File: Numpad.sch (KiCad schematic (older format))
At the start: 51 parts, among them J1 USB_B_Mini, SW0 0, SW1 1, SW2 2, SW3 3, SW4 4, SW5 5, SW6 6, SW7 7, SW8 8, SW9 9, U1 ATmega32U4-AU, Y1 16MHz

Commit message: plate files added, moved around some more components
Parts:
- C6: value 0.1uF -> 1uF
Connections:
- net Col1: now also U1.29 (PB5); no longer U1.18 (PD0)
- net Col2: now also U1.28 (PB4); no longer U1.19 (PD1)
- net Col3: now also U1.26 (PD6); no longer U1.20 (PD2)
- net Col4: now also U1.25 (PD4); no longer U1.21 (PD3)
- net Row1: now also U1.41 (PF0); no longer U1.8 (PB0)
- net Row2: now also U1.40 (PF1); no longer U1.9 (PB1)
- net Row3: now also U1.39 (PF4); no longer U1.10 (PB2)
- net Row4: now also U1.38 (PF5); no longer U1.11 (PB3)
- net Row5: now also U1.37 (PF6); no longer U1.28 (PB4)
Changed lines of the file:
@@
 	0    -1   -1   0
-$EndComp
-$Comp
-L Device:C_Small C5
-U 1 1 5D759123
-P 3600 1300
-F 0 "C5" V 3829 1300 50  0000 C CNN
-F 1 "10uF" V 3738 1300 50  0000 C CNN
-F 2 "Capacitor_SMD:C_0805_2012Metric_Pad1.15x1.40mm_HandSolder" H 3600 1300 50  0001 C CNN
-F 3 "~" H 3600 1300 50  0001 C CNN
-	1    3600 1300
-	-1   0    0    1
-$EndComp
-$Comp
-L Device:C_Small C6
-U 1 1 5D759CD2
-P 3950 1300
-F 0 "C6" V 4179 1300 50  0000 C CNN
-F 1 "0.1uF" V 4088 1300 50  0000 C CNN
-F 2 "Capacitor_SMD:C_0805_2012Metric_Pad1.15x1.40mm_HandSolder" H 3950 1300 50  0001 C CNN
-F 3 "~" H 3950 1300 50  0001 C CNN
-	1    3950 1300
-	-1   0    0    1
-$EndComp
-$Comp
-L Device:C_Small C8
-U 1 1 5D75B0ED
-P 4650 1300
-F 0 "C8" V 4879 1300 50  0000 C CNN
-F 1 "01.uF" V 4788 1300 50  0000 C CNN
-F 2 "Capacitor_SMD:C_0805_2012Metric_Pad1.15x1.40mm_HandSolder" H 4650 1300 50  0001 C CNN
-F 3 "~" H 4650 1300 50  0001 C CNN
-	1    4650 1300
-	-1   0    0    1
 $EndComp
 Wire Wire Line
@@
 	4650 1600 4300 1600
 Connection ~ 4300 1600
-$Comp
-L Device:C_Small C7
-U 1 1 5D75A7CA
-P 4300 1300
-F 0 "C7" V 4529 1300 50  0000 C CNN
-F 1 "0.1uF" V 4438 1300 50  0000 C CNN
-F 2 "Capacitor_SMD:C_0805_2012Metric_Pad1.15x1.40mm_HandSolder" H 4300 1300 50  0001 C CNN
-F 3 "~" H 4300 1300 50  0001 C CNN
-	1    4300 1300
-	-1   0    0    1
-$EndComp
 $Comp
 L Device:R_Small R1
@@
 Wire Wire Line
 	2600 6900 2600 6800
-Text GLabel 1300 5300 1    50   Output ~ 0
+Text GLabel 3700 5300 1    50   Output ~ 0
 Row1
-Text GLabel 1400 5300 1    50   Output ~ 0
+Text GLabel 3800 5300 1    50   Output ~ 0
 Row2
-Text GLabel 1500 5300 1    50   Output ~ 0
+Text GLabel 3900 5300 1    50   Output ~ 0
 Row3
-Text GLabel 1600 5300 1    50   Output ~ 0
+Text GLabel 4000 5300 1    50   Output ~ 0
 Row4
+Text GLabel 4100 5300 1    50   Output ~ 0
+Row5
+Text GLabel 1800 5300 1    50   Output ~ 0
+Col1
 Text GLabel 1700 5300 1    50   Output ~ 0
-Row5
-Text GLabel 2500 5300 1    50   Output ~ 0
-Col1
-Text GLabel 2600 5300 1    50   Output ~ 0
 Col2
-Text GLabel 2700 5300 1    50   Output ~ 0
+Text GLabel 3100 5300 1    50   Output ~ 0
 Col3
-Text GLabel 2800 5300 1    50   Output ~ 0
+Text GLabel 2900 5300 1    50   Output ~ 0
 Col4
 Text GLabel 2300 6500 3    50   Input ~ 0
@@
 Wire Wire Line
 	2850 2700 2850 2550
+$Comp
+L Device:C_Small C8
+U 1 1 5D75B0ED
+P 4650 1300
+F 0 "C8" V 4879 1300 50  0000 C CNN
+F 1 "01.uF" V 4788 1300 50  0000 C CNN
+F 2 "Capacitor_SMD:C_0805_2012Metric_Pad1.15x1.40mm_HandSolder" H 4650 1300 50  0001 C CNN
+F 3 "~" H 4650 1300 50  0001 C CNN
+	1    4650 1300
+	-1   0    0    1
+$EndComp
+$Comp
+L Device:C_Small C7
+U 1 1 5D75A7CA
+P 4300 1300
+F 0 "C7" V 4529 1300 50  0000 C CNN
+F 1 "0.1uF" V 4438 1300 50  0000 C CNN
+F 2 "Capacitor_SMD:C_0805_2012Metric_Pad1.15x1.40mm_HandSolder" H 4300 1300 50  0001 C CNN
+F 3 "~" H 4300 1300 50  0001 C CNN
+	1    4300 1300
+	-1   0    0    1
+$EndComp
+$Comp
+L Device:C_Small C6
+U 1 1 5D759CD2
+P 3950 1300
+F 0 "C6" V 4179 1300 50  0000 C CNN
+F 1 "1uF" V 4088 1300 50  0000 C CNN
+F 2 "Capacitor_SMD:C_0805_2012Metric_Pad1.15x1.40mm_HandSolder" H 3950 1300 50  0001 C CNN
+F 3 "~" H 3950 1300 50  0001 C CNN
+	1    3950 1300
+	-1   0    0    1
+$EndComp
+$Comp
+L Device:C_Small C5
+U 1 1 5D759123
+P 3600 1300
+F 0 "C5" V 3829 1300 50  0000 C CNN
+F 1 "10uF" V 3738 1300 50  0000 C CNN
+F 2 "Capacitor_SMD:C_0805_2012Metric_Pad1.15x1.40mm_HandSolder" H 3600 1300 50  0001 C CNN
+F 3 "~" H 3600 1300 50  0001 C CNN
+	1    3600 1300
+	-1   0    0    1
+$EndComp
 $EndSCHEMATC

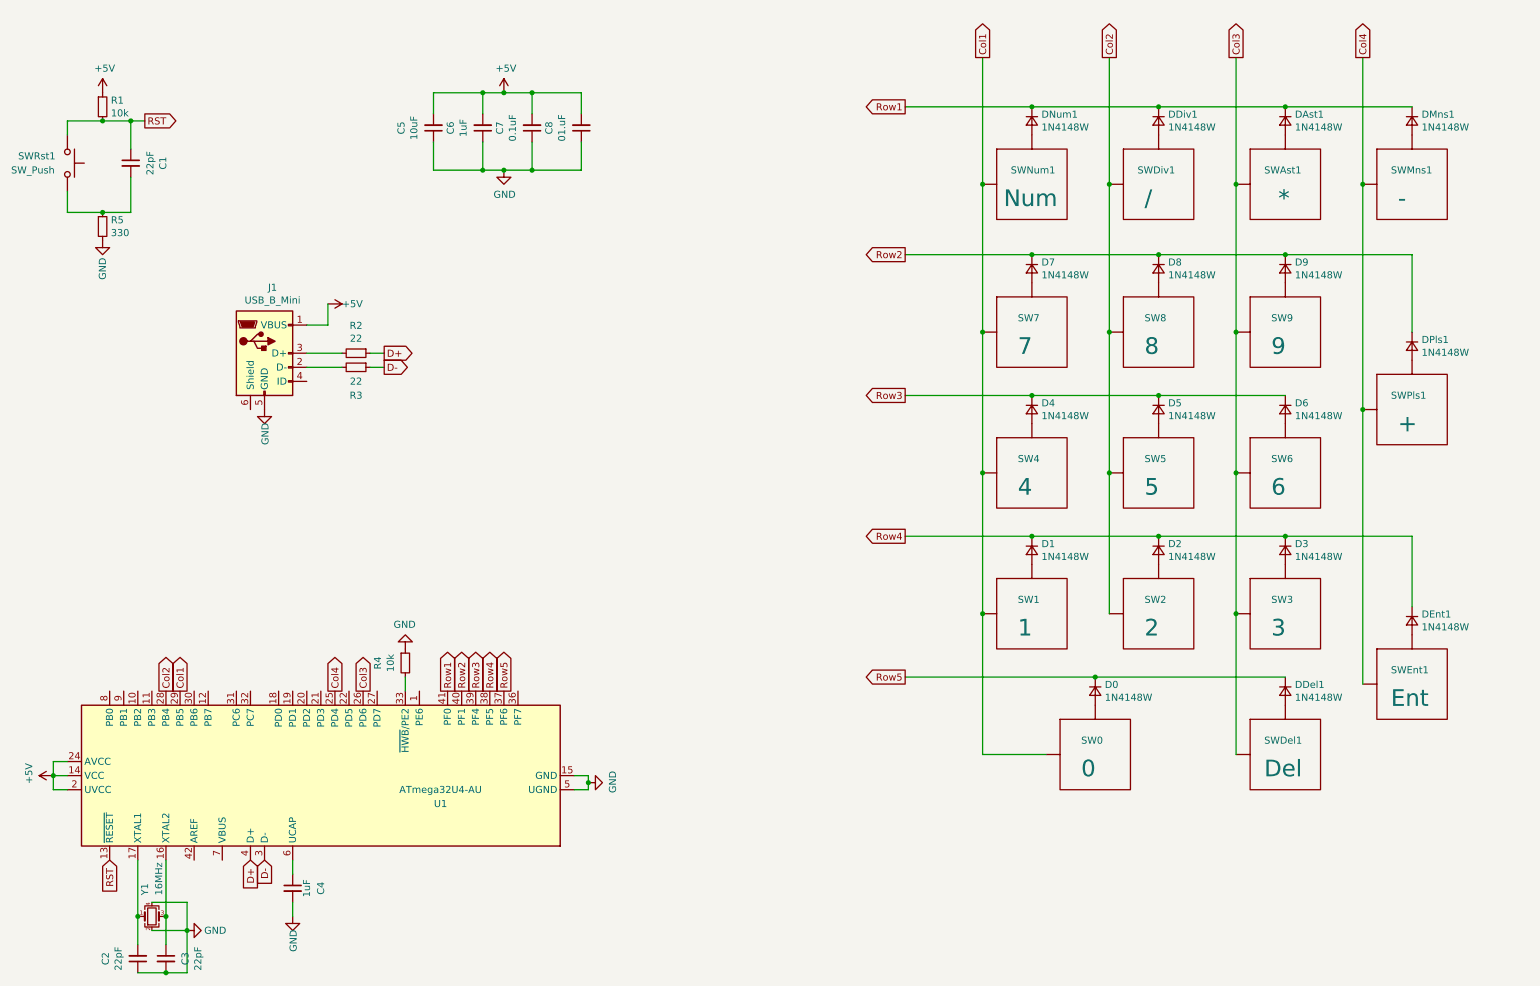
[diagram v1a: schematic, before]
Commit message: allowed split + key
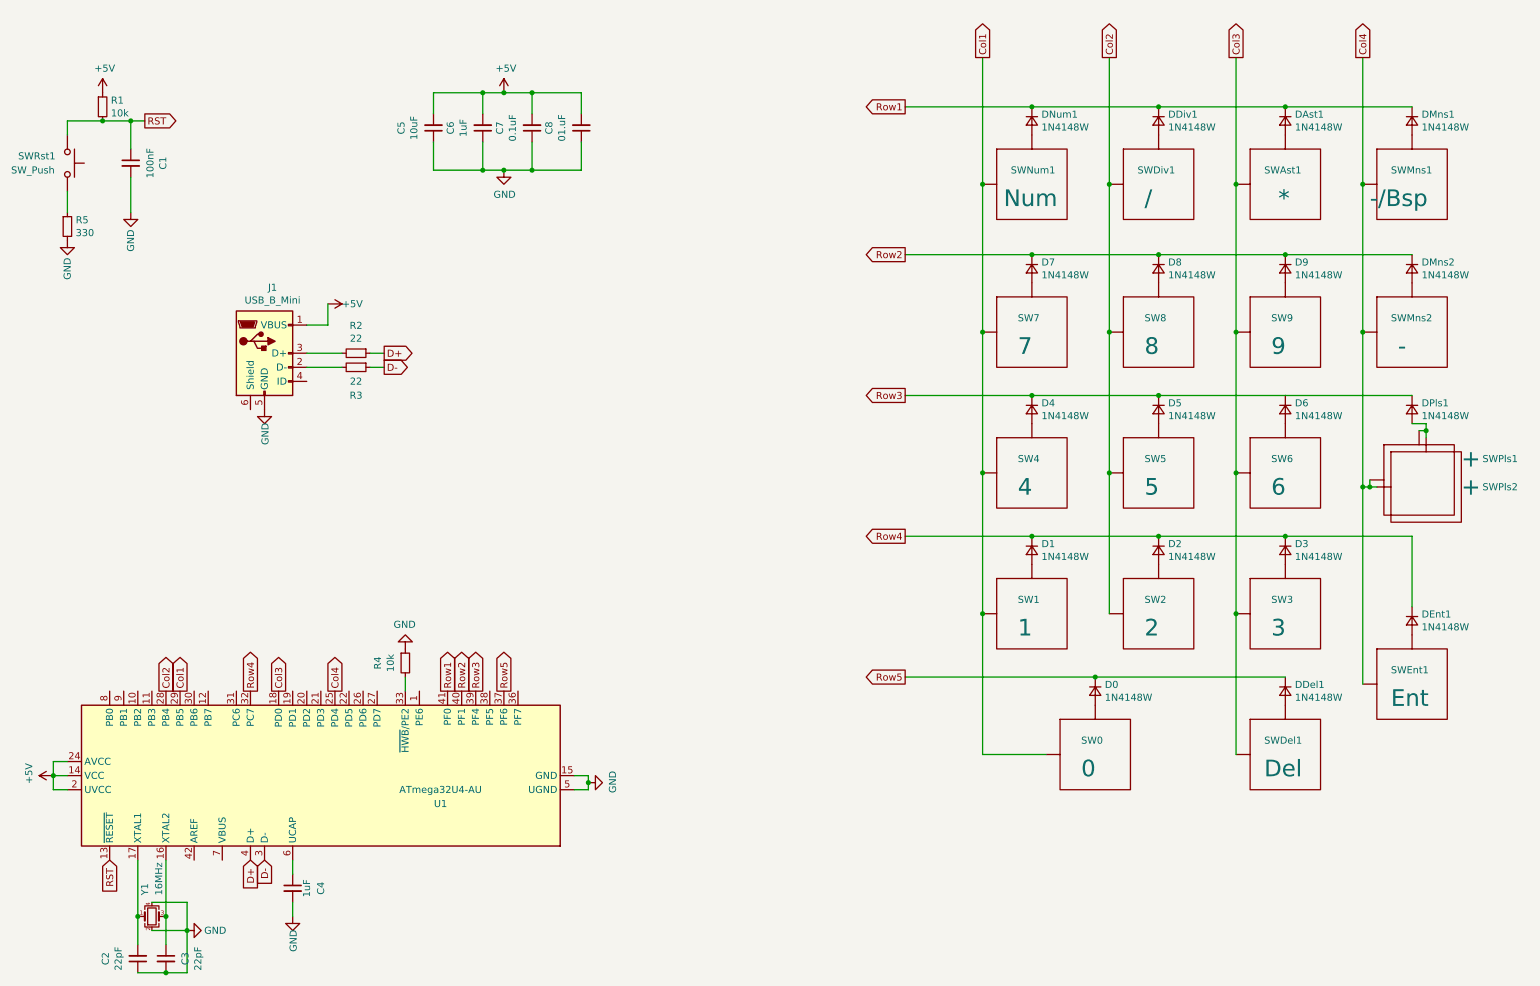
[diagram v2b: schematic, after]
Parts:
- added DPls1: 1N4148W, Diode_SMD:D_0603_1608Metric_Pad1.05x0.95mm_HandSolder, symbol Device:D_Small
- added SWMns2: -, AcheronMX:MX100, symbol Acheron:MXSwitch
- added SWPls2: +, AcheronMX:MX100, symbol Acheron:MXSwitch
- C1: value 22pF -> 100nF; footprint Capacitor_SMD:C_0805_2012Metric_Pad1.15x1.40mm_HandSolder -> Capacitor_SMD:C_0603_1608Metric_Pad1.05x0.95mm_HandSolder
- C2, C3, C4, C5, C6, C7, C8: footprint Capacitor_SMD:C_0805_2012Metric_Pad1.15x1.40mm_HandSolder -> Capacitor_SMD:C_0603_1608Metric_Pad1.05x0.95mm_HandSolder
- D0, D1, D2, D3, D4, D5, D6, D7, D8, D9, DAst1, DDel1, DDiv1, DEnt1, DMns1, DNum1: footprint Diode_SMD:D_SOD-123 -> Diode_SMD:D_0603_1608Metric_Pad1.05x0.95mm_HandSolder
- DMns2: renamed from DPls1; footprint Diode_SMD:D_SOD-123 -> Diode_SMD:D_0603_1608Metric_Pad1.05x0.95mm_HandSolder
- R1, R2, R3, R4, R5: footprint Resistor_SMD:R_1206_3216Metric_Pad1.42x1.75mm_HandSolder -> Resistor_SMD:R_0603_1608Metric_Pad1.05x0.95mm_HandSolder
- SWMns1: value - -> -/Bsp
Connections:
- net Col3: now also U1.18 (PD0); no longer U1.26 (PD6)
- net Col4: now also SWMns2.1 (Col), SWPls2.1 (Col)
- net GND: now also C1.2
- net Row3: now also DPls1.1 (K)
- net Row4: now also U1.32 (PC7); no longer U1.38 (PF5)
- net at R5.1, SWRst1.2: no longer C1.2
- net at SWPls1.2 (Row): now also DPls1.2 (A), SWPls2.2 (Row); no longer DMns2.2 (A)
- new net: DMns2.2 (A), SWMns2.2 (Row)
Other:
- moved on the sheet: DMns2, R5, SWPls1

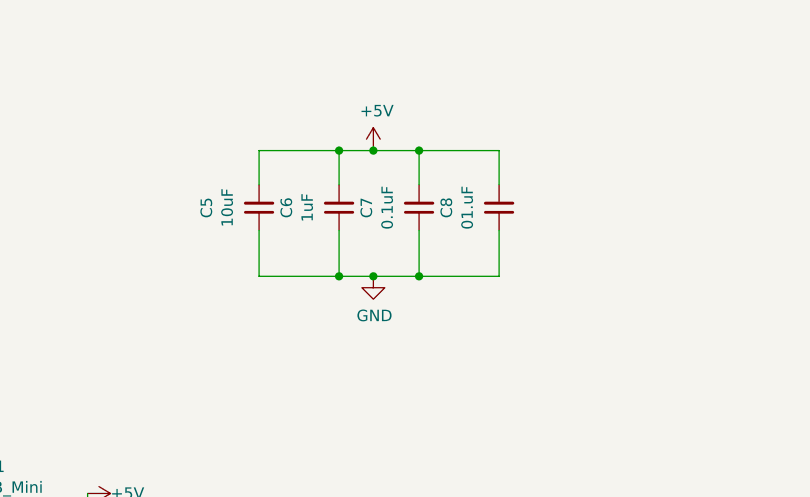
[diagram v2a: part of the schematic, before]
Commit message: all componentes withing the confines of the board now, still need to add ground. Not shure about the components around reset button or c5 & c9's grounding
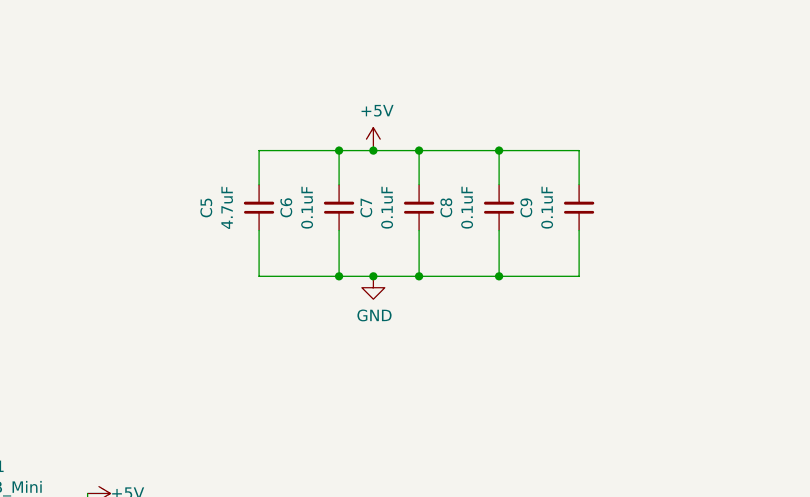
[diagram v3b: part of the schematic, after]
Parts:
- added C9: 0.1uF, Capacitor_SMD:C_0603_1608Metric_Pad1.05x0.95mm_HandSolder, symbol Device:C_Small
- C5: value 10uF -> 4.7uF
- C6: value 1uF -> 0.1uF
- C8: value 01.uF -> 0.1uF
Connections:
- net +5V: now also C9.2
- net GND: now also C9.1
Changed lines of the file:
@@
 P 4650 1300
 F 0 "C8" V 4879 1300 50  0000 C CNN
-F 1 "01.uF" V 4788 1300 50  0000 C CNN
+F 1 "0.1uF" V 4788 1300 50  0000 C CNN
 F 2 "Capacitor_SMD:C_0603_1608Metric_Pad1.05x0.95mm_HandSolder" H 4650 1300 50  0001 C CNN
 F 3 "~" H 4650 1300 50  0001 C CNN
@@
 P 3950 1300
 F 0 "C6" V 4179 1300 50  0000 C CNN
-F 1 "1uF" V 4088 1300 50  0000 C CNN
+F 1 "0.1uF" V 4088 1300 50  0000 C CNN
 F 2 "Capacitor_SMD:C_0603_1608Metric_Pad1.05x0.95mm_HandSolder" H 3950 1300 50  0001 C CNN
 F 3 "~" H 3950 1300 50  0001 C CNN
@@
 P 3600 1300
 F 0 "C5" V 3829 1300 50  0000 C CNN
-F 1 "10uF" V 3738 1300 50  0000 C CNN
+F 1 "4.7uF" V 3738 1300 50  0000 C CNN
 F 2 "Capacitor_SMD:C_0603_1608Metric_Pad1.05x0.95mm_HandSolder" H 3600 1300 50  0001 C CNN
 F 3 "~" H 3600 1300 50  0001 C CNN
@@
 Wire Wire Line
 	10250 3850 10200 3850
+Wire Wire Line
+	5000 1200 5000 1050
+Wire Wire Line
+	5000 1050 4650 1050
+Wire Wire Line
+	5000 1400 5000 1600
+Wire Wire Line
+	5000 1600 4650 1600
+$Comp
+L Device:C_Small C9
+U 1 1 5DA64870
+P 5000 1300
+F 0 "C9" V 5229 1300 50  0000 C CNN
+F 1 "0.1uF" V 5138 1300 50  0000 C CNN
+F 2 "Capacitor_SMD:C_0603_1608Metric_Pad1.05x0.95mm_HandSolder" H 5000 1300 50  0001 C CNN
+F 3 "~" H 5000 1300 50  0001 C CNN
+	1    5000 1300
+	-1   0    0    1
+$EndComp
+Connection ~ 4650 1050
+Connection ~ 4650 1600
 $EndSCHEMATC
